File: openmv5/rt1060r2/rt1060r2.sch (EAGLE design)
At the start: 254 parts, among them CN1 S2B-PH-K-S(LF)(SN), IC1 LM66200DRLR, IC2 TCR2LF33,LM_CT, IC3 AP61300Z6-7, IC4 IS42S16160G-6BL, IC5 IS25LP128F-JKLE-TR, IC6 SE050C1HQ1_Z01SCZ, IC7 MXC4005XC, IC8 KSZ8081RNDCA-TR, IC9 MIMXRT106FCVL5B, J1 USB4105-GF-A, J2 USD-1040310811, J3 DF12-36-DS, J4 DNP, J5 DNP, J6 DNP, J7 DNP, J8 3221-10-0300-00, J9 DNP, M1 9774030151R, M2 9774030151R, Q1 DMG2301L-7, Q2 2N7002KW_R1_00001, Q3 2N7002KW_R1_00001, Q4 2N7002KW_R1_00001, U1 BQ24075RGTR, U2 LBEE5KL1DX-883, Y1 ECS-327MVATX-3-CN-TR3, Y2 XRCGB24M000F3M00R0, Y3 SC32S-7PF20PPM

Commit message: Fix some issues with MPN and extra lablels
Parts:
- IC6: MPN (none) -> SE050C1HQ1/Z01SCZ
- R42, R43: MPN AC0402FR-1310KL -> CRCW04021K00FKEDC
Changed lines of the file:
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@@
 <part name="P+19" library="SparkFun" deviceset="VCC" device=""/>
 <part name="R42" library="0402" deviceset="RES_0402" device="" value="1K">
-<attribute name="MPN" value="AC0402FR-1310KL"/>
+<attribute name="MPN" value="CRCW04021K00FKEDC"/>
 </part>
 <part name="R43" library="0402" deviceset="RES_0402" device="" value="1K">
-<attribute name="MPN" value="AC0402FR-1310KL"/>
+<attribute name="MPN" value="CRCW04021K00FKEDC"/>
 </part>
 <part name="P+23" library="SparkFun" deviceset="VCC" device=""/>
@@
 </part>
 <part name="GND42" library="sfe" deviceset="GND" device=""/>
-<part name="IC6" library="SE050C1HQ1_Z01SCZ" deviceset="SE050C1HQ1_Z01SCZ" device=""/>
+<part name="IC6" library="SE050C1HQ1_Z01SCZ" deviceset="SE050C1HQ1_Z01SCZ" device="">
+<attribute name="MPN" value="SE050C1HQ1/Z01SCZ"/>
+</part>
 <part name="GND43" library="sfe" deviceset="GND" device=""/>
 <part name="C111" library="0402" deviceset="CAP_0402" device="" value="0.1uF">
@@
 <attribute name="NAME" x="62.23" y="127" size="1.778" layer="95" align="center-left"/>
 <attribute name="VALUE" x="62.23" y="124.46" size="1.778" layer="96" align="center-left"/>
+<attribute name="MPN" x="15.24" y="101.6" size="1.778" layer="96" display="off"/>
 </instance>
 <instance part="GND43" gate="1" x="12.7" y="50.8" smashed="yes" rot="MR0">

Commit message: Update diodes
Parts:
- removed D3, D4: RB521S30T5G, RB521S30T5G:RB521S30T5G
- added C113: 4.7uF, 0402:CAP_0402
- added D15: BAT54CLT3G, BAT54CLT3G:BAT54CLT3G
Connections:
- net GND: now also C113.1
- net SNVS_BAT: now also D15.A2; no longer D4.A
- net VCC: now also C113.2
- net VDD_SNVS: now also D15.A1; no longer D3.A
- net VDD_SNVS_CPU: now also D15.K; no longer D3.K, D4.K
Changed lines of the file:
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@@
 <attribute name="MPN" value="MFBM1V1005-101-R"/>
 </part>
-<part name="D3" library="RB521S30T5G" deviceset="RB521S30T5G" device="">
-<attribute name="MPN" value="RB521S30T5G"/>
-</part>
-<part name="D4" library="RB521S30T5G" deviceset="RB521S30T5G" device="">
-<attribute name="MPN" value="RB521S30T5G"/>
-</part>
 <part name="TP1" library="testpad" library_urn="urn:adsk.eagle:library:385" deviceset="TP" device="TP10R" package3d_urn="urn:adsk.eagle:package:27959/1" value="TPTP10R"/>
 <part name="TP2" library="testpad" library_urn="urn:adsk.eagle:library:385" deviceset="TP" device="TP10R" package3d_urn="urn:adsk.eagle:package:27959/1" value="TPTP10R"/>
@@
 <attribute name="MPN" value="JMK105BBJ475MV-F"/>
 </part>
+<part name="C113" library="0402" deviceset="CAP_0402" device="" value="4.7uF">
+<attribute name="MPN" value="JMK105BBJ475MV-F"/>
+</part>
+<part name="GND44" library="SparkFun" deviceset="GND" device=""/>
+<part name="D15" library="BAT54CLT3G" deviceset="BAT54CLT3G" device=""/>
 </parts>
 <sheets>
@@
 <text x="121.92" y="88.9" size="1.778" layer="97">BAT_3.3V</text>
 <text x="121.92" y="78.74" size="1.778" layer="97">BAT_GND</text>
-<text x="124.46" y="114.3" size="1.778" layer="97" rot="R180">3.3V</text>
+<text x="144.78" y="114.3" size="1.778" layer="97" rot="R180">3.3V</text>
 </plain>
 <instances>
@@
 <attribute name="MPN" x="215.9" y="137.16" size="1.778" layer="96" rot="R270" display="off"/>
 </instance>
-<instance part="D3" gate="G$1" x="106.68" y="119.38" smashed="yes" rot="R90">
-<attribute name="NAME" x="109.22" y="123.19" size="1.778" layer="95" align="center-left"/>
-<attribute name="VALUE" x="109.22" y="120.65" size="1.778" layer="96" align="center-left"/>
-<attribute name="MPN" x="106.68" y="119.38" size="1.778" layer="96" rot="R90" display="off"/>
-</instance>
-<instance part="D4" gate="G$1" x="106.68" y="114.3" smashed="yes" rot="R270">
-<attribute name="NAME" x="104.14" y="110.49" size="1.778" layer="95" rot="R180" align="center-left"/>
-<attribute name="VALUE" x="104.14" y="113.03" size="1.778" layer="96" rot="R180" align="center-left"/>
-<attribute name="MPN" x="106.68" y="114.3" size="1.778" layer="96" rot="R270" display="off"/>
-</instance>
 <instance part="TP1" gate="G$1" x="119.38" y="86.36" smashed="yes" rot="R270">
 <attribute name="NAME" x="120.65" y="87.63" size="1.778" layer="95" rot="R270"/>
@@
 <attribute name="VALUE" x="139.7" y="60.96" size="1.778" layer="96" rot="MR0"/>
 </instance>
+<instance part="D15" gate="G$1" x="101.6" y="116.84" smashed="yes">
+<attribute name="NAME" x="120.65" y="124.46" size="1.778" layer="95" align="center-left"/>
+<attribute name="VALUE" x="120.65" y="121.92" size="1.778" layer="96" align="center-left"/>
+</instance>
 </instances>
 <busses>
@@
 <wire x1="96.52" y1="152.4" x2="96.52" y2="144.78" width="0.1524" layer="91"/>
 <label x="96.52" y="152.4" size="1.778" layer="95"/>
-<wire x1="96.52" y1="144.78" x2="106.68" y2="144.78" width="0.1524" layer="91"/>
+<wire x1="96.52" y1="144.78" x2="101.6" y2="144.78" width="0.1524" layer="91"/>
 <wire x1="96.52" y1="114.3" x2="96.52" y2="144.78" width="0.1524" layer="91"/>
 <junction x="96.52" y="114.3"/>
 <junction x="96.52" y="144.78"/>
-<pinref part="D3" gate="G$1" pin="A"/>
-<wire x1="106.68" y1="144.78" x2="106.68" y2="137.16" width="0.1524" layer="91"/>
+<pinref part="D15" gate="G$1" pin="A1"/>
+<wire x1="101.6" y1="116.84" x2="101.6" y2="144.78" width="0.1524" layer="91"/>
 </segment>
 </net>
@@
 <segment>
 <pinref part="TP1" gate="G$1" pin="TP"/>
-<wire x1="116.84" y1="86.36" x2="106.68" y2="86.36" width="0.1524" layer="91"/>
-<pinref part="D4" gate="G$1" pin="A"/>
-<wire x1="106.68" y1="86.36" x2="106.68" y2="96.52" width="0.1524" layer="91"/>
+<wire x1="116.84" y1="86.36" x2="101.6" y2="86.36" width="0.1524" layer="91"/>
+<pinref part="D15" gate="G$1" pin="A2"/>
+<wire x1="101.6" y1="86.36" x2="101.6" y2="114.3" width="0.1524" layer="91"/>
 </segment>
 </net>
 <net name="VDD_SNVS_CPU" class="0">
 <segment>
-<pinref part="D4" gate="G$1" pin="K"/>
-<pinref part="D3" gate="G$1" pin="K"/>
-<wire x1="106.68" y1="111.76" x2="106.68" y2="116.84" width="0.1524" layer="91"/>
-<wire x1="106.68" y1="116.84" x2="106.68" y2="121.92" width="0.1524" layer="91"/>
-<wire x1="106.68" y1="116.84" x2="127" y2="116.84" width="0.1524" layer="91"/>
-<junction x="106.68" y="116.84"/>
-<label x="127" y="116.84" size="1.778" layer="95" rot="R180"/>
+<wire x1="124.46" y1="116.84" x2="144.78" y2="116.84" width="0.1524" layer="91"/>
+<label x="144.78" y="116.84" size="1.778" layer="95" rot="R180"/>
+<pinref part="D15" gate="G$1" pin="K"/>
 </segment>
 </net>
@@
 <attribute name="MPN" x="66.04" y="76.2" size="1.778" layer="96" rot="R90" display="off"/>
 </instance>
+<instance part="C113" gate="G$1" x="10.16" y="106.68" smashed="yes" rot="R180">
+<attribute name="NAME" x="8.636" y="101.219" size="1.778" layer="95" rot="R180"/>
+<attribute name="VALUE" x="8.636" y="106.299" size="1.778" layer="96" rot="R180"/>
+<attribute name="MPN" x="10.16" y="106.68" size="1.778" layer="96" rot="R180" display="off"/>
+</instance>
+<instance part="GND44" gate="1" x="10.16" y="91.44" smashed="yes" rot="MR0">
+<attribute name="VALUE" x="12.7" y="88.9" size="1.778" layer="96" rot="MR0"/>
+</instance>
 </instances>
 <busses>
@@
 <pinref part="GND36" gate="1" pin="GND"/>
 </segment>
+<segment>
+<pinref part="GND44" gate="1" pin="GND"/>
+<pinref part="C113" gate="G$1" pin="1"/>
+<wire x1="10.16" y1="93.98" x2="10.16" y2="99.06" width="0.1524" layer="91"/>
+</segment>
 </net>
 <net name="VCC" class="0">
@@
 <junction x="15.24" y="114.3"/>
 <junction x="15.24" y="111.76"/>
+<pinref part="C113" gate="G$1" pin="2"/>
+<wire x1="10.16" y1="106.68" x2="10.16" y2="114.3" width="0.1524" layer="91"/>
+<wire x1="10.16" y1="114.3" x2="15.24" y2="114.3" width="0.1524" layer="91"/>
 </segment>
 <segment>

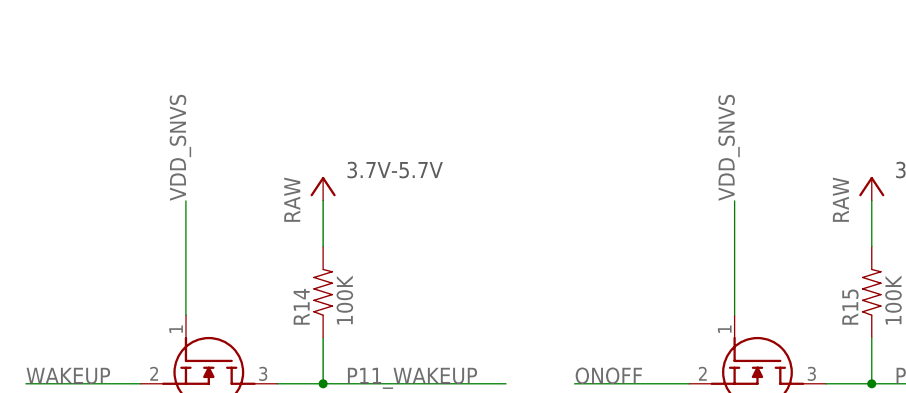
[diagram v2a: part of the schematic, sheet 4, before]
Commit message: Fix possible low power mode leakage
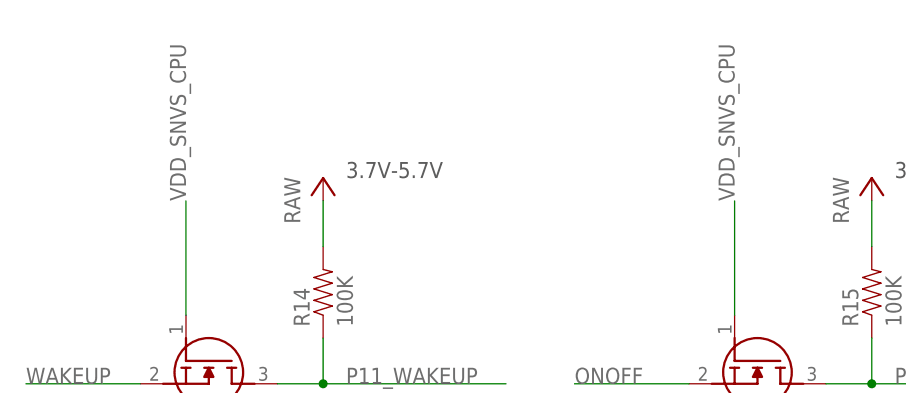
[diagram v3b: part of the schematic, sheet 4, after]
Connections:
- net VDD_SNVS: no longer Q2.G, Q3.G, Q4.G
- net VDD_SNVS_CPU: now also Q2.G, Q3.G, Q4.G
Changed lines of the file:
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@@
 <net name="VDD_SNVS" class="0">
-<segment>
-<wire x1="154.94" y1="137.16" x2="154.94" y2="149.86" width="0.1524" layer="91"/>
-<pinref part="Q2" gate="G$1" pin="G"/>
-<label x="154.94" y="149.86" size="1.778" layer="95" rot="R90"/>
-</segment>
-<segment>
-<wire x1="215.9" y1="137.16" x2="215.9" y2="149.86" width="0.1524" layer="91"/>
-<pinref part="Q3" gate="G$1" pin="G"/>
-<label x="215.9" y="149.86" size="1.778" layer="95" rot="R90"/>
-</segment>
 <segment>
 <wire x1="78.74" y1="114.3" x2="96.52" y2="114.3" width="0.1524" layer="91"/>
@@
 <label x="144.78" y="116.84" size="1.778" layer="95" rot="R180"/>
 <pinref part="D15" gate="G$1" pin="K"/>
+</segment>
+<segment>
+<wire x1="154.94" y1="137.16" x2="154.94" y2="149.86" width="0.1524" layer="91"/>
+<pinref part="Q2" gate="G$1" pin="G"/>
+<label x="154.94" y="149.86" size="1.778" layer="95" rot="R90"/>
+</segment>
+<segment>
+<wire x1="215.9" y1="137.16" x2="215.9" y2="149.86" width="0.1524" layer="91"/>
+<pinref part="Q3" gate="G$1" pin="G"/>
+<label x="215.9" y="149.86" size="1.778" layer="95" rot="R90"/>
 </segment>
 </net>
@@
 </segment>
 </net>
-<net name="VDD_SNVS" class="0">
+<net name="VDD_SNVS_CPU" class="0">
 <segment>
 <pinref part="Q4" gate="G$1" pin="G"/>

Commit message: Update processor
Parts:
- IC9: value MIMXRT106FCVL5B -> MIMXRT106FDVL6B; DESCRIPTION Processors - Application Specialized MIMXRT1062DVL6B/LFBGA1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 -> Processors - Application Specialized MIMXRT106FDVL6B/LFBGA1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; MANUFACTURER_PART_NUMBER MIMXRT1062DVL6B -> MIMXRT106FDVL6B; MOUSER_PART_NUMBER 771-MIMXRT1062DVL6B -> 771-MIMXRT106FDVL6B; MOUSER_PRICE-STOCK https://www.mouser.co.uk/ProductDetail/NXP-Semiconductors/MIMXRT1062DVL6B -> https://www.mouser.co.uk/ProductDetail/NXP-Semiconductors/MIMXRT106FDVL6B; MPN MIMXRT106FCVL5B -> MIMXRT106FDVL6B
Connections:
- net RST_BUTTON renamed ONOFF_BUTTON
- net ONOFF: now also R70.1
- net P12_RST_N: no longer R70.1
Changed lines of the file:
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@@
 </part>
 <part name="P+1" library="SparkFun" deviceset="VCC" device=""/>
-<part name="IC9" library="MIMXRT1052DVL6B" deviceset="MIMXRT1052DVL6B" device="" value="MIMXRT106FCVL5B">
-<attribute name="DESCRIPTION" value="Processors - Application Specialized MIMXRT1062DVL6B/LFBGA196///STANDARD MARKING * TRAY"/>
-<attribute name="MANUFACTURER_PART_NUMBER" value="MIMXRT1062DVL6B"/>
-<attribute name="MOUSER_PART_NUMBER" value="771-MIMXRT1062DVL6B"/>
-<attribute name="MOUSER_PRICE-STOCK" value="https://www.mouser.co.uk/ProductDetail/NXP-Semiconductors/MIMXRT1062DVL6B"/>
-<attribute name="MPN" value="MIMXRT106FCVL5B"/>
+<part name="IC9" library="MIMXRT1052DVL6B" deviceset="MIMXRT1052DVL6B" device="" value="MIMXRT106FDVL6B">
+<attribute name="DESCRIPTION" value="Processors - Application Specialized MIMXRT106FDVL6B/LFBGA196///STANDARD MARKING * TRAY"/>
+<attribute name="MANUFACTURER_PART_NUMBER" value="MIMXRT106FDVL6B"/>
+<attribute name="MOUSER_PART_NUMBER" value="771-MIMXRT106FDVL6B"/>
+<attribute name="MOUSER_PRICE-STOCK" value="https://www.mouser.co.uk/ProductDetail/NXP-Semiconductors/MIMXRT106FDVL6B"/>
+<attribute name="MPN" value="MIMXRT106FDVL6B"/>
 </part>
 <part name="C32" library="SparkFun-Capacitors" library_urn="urn:adsk.eagle:library:510" deviceset="22UF" device="-0805-6.3V-20%" package3d_urn="urn:adsk.eagle:package:37429/1" value="22uF">
@@
 <pinref part="Q3" gate="G$1" pin="S"/>
 </segment>
+<segment>
+<pinref part="R70" gate="G$1" pin="1"/>
+<wire x1="187.96" y1="83.82" x2="208.28" y2="83.82" width="0.1524" layer="91"/>
+<label x="190.5" y="83.82" size="1.778" layer="95"/>
+</segment>
 </net>
 <net name="SNVS_BAT" class="0">
@@
 </segment>
 </net>
-<net name="RST_BUTTON" class="0">
+<net name="ONOFF_BUTTON" class="0">
 <segment>
 <pinref part="S2" gate="G$1" pin="COM_2"/>
@@
 </segment>
 </net>
-<net name="P12_RST_N" class="0">
-<segment>
-<pinref part="R70" gate="G$1" pin="1"/>
-<wire x1="187.96" y1="83.82" x2="208.28" y2="83.82" width="0.1524" layer="91"/>
-<label x="190.5" y="83.82" size="1.778" layer="95"/>
-</segment>
-</net>
